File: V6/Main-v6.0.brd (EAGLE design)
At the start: 80 x 80 mm, 116 parts, among them IC1 MC34063AD, J11 AVR_SPI_PROG_3X2NS, M01 JUMPER-SMT_2_NC_PASTE_SILK, M02 JUMPER-SMT_2_NC_PASTE_SILK, M11 JUMPER-SMT_2_NC_PASTE_SILK, M12 JUMPER-SMT_2_NC_PASTE_SILK, Q1 MOSFET-NCHANNEL2N7002PW, Q2 MOSFET-NCHANNEL2N7002PW, U1 ULN2803ADWG4, U10 FSMSMTR, U2 ULN2803ADWG4, U3 UA7805CKTTR, U4 DRV8834RGERTSSOP, U5 DRV8834RGERTSSOP, U7 ATMEGA328P_TQFP, U8 SSA12, U9 FSMSMTR, X1 FH12-16S-1SH, Y1 16MHZ

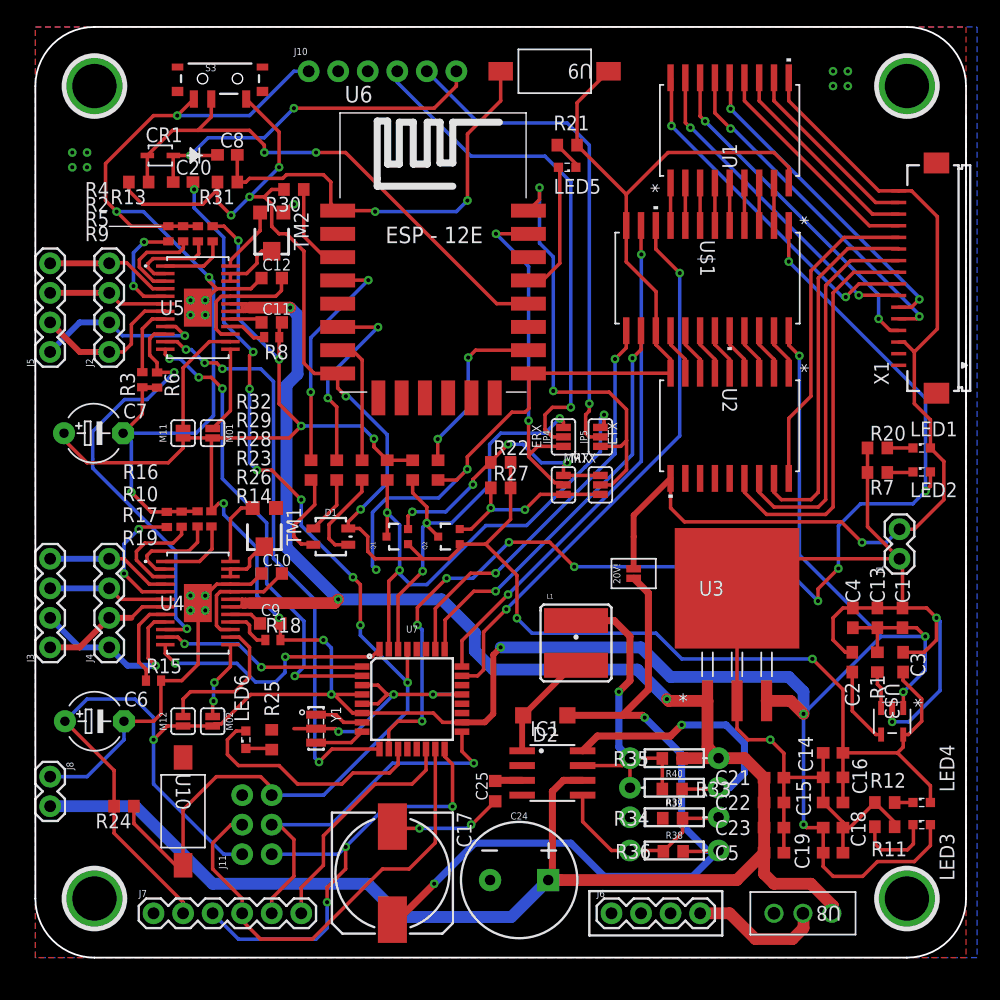
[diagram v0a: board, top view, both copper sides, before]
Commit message: Updated silkscreen in V5.1 and voltage booster is replaced in V6.0
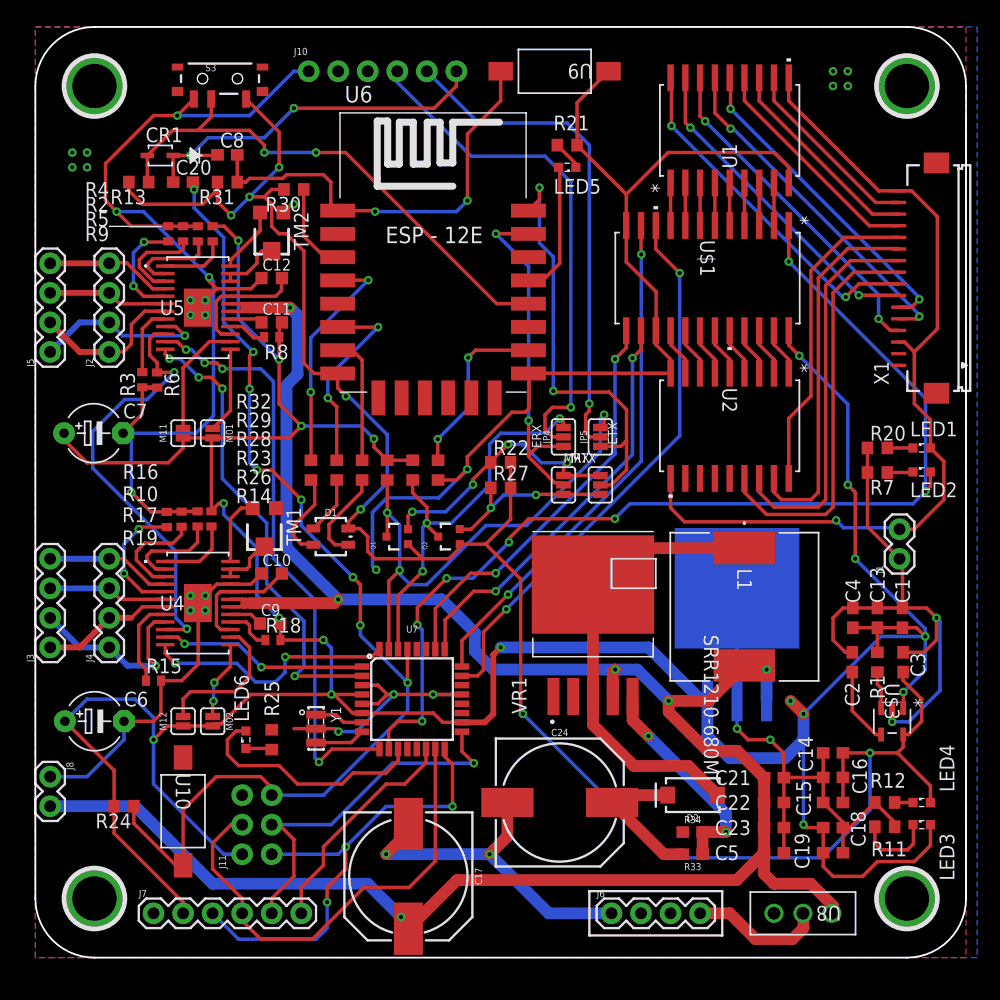
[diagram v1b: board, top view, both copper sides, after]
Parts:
- removed 20V!: JUMPER-SMT_2_NC_PASTE_NO-SILK, SparkFun-Jumpers:SMT-JUMPER_2_NC_PASTE_NO-SILK
- removed C25: 1.5nF, resistor:C0603K
- removed IC1: MC34063AD, MC34063A:SO08
- removed R35: 0.22R, resistor:R0603
- removed R36: 33k, resistor:R0603
- removed R37, R38, R39, R40: (no value), SparkFun-Resistors:AXIAL-0.3
- added VR1: XL6009, XL6009:DPAK170P1435X465-6N
- C17: value 330uF -> 220uF; device resistor:153CLV-1010 -> SparkFun-Capacitors:NIC_10X10.5_CAP
- C24: device SparkFun-Capacitors:CPOL-RADIAL-5MM-10MM -> SparkFun-Capacitors:NIC_10X10.5_CAP
- D2: value 1N5819 -> 3A/40V/500mV; device Beeclust:SOD123 -> SparkFun-DiscreteSemi:SMA-DIODE
- L1: value 180uH -> SRR1210-680M; device adjacent-reality:CR54 -> 12MM Inductor:IND_BOURNS_SRR1210
- R33: value 180R -> (none); device resistor:R0603 -> SparkFun-Resistors:0603
- R34: value 2.2k -> (none); device resistor:R0603 -> SparkFun-Resistors:0603
- moved L1 14.8 mm to (61.0, 30.2), turned to 270 degrees
- moved D2 14.4 mm to (56.5, 14.0)
- moved C24 7.53 mm to (45.1, 13.3)
- moved R33 5.87 mm to (56.5, 8.89)
- moved R34 2.09 mm to (56.5, 10.8)
- moved C17 1.40 mm to (32.1, 6.99)
- flipped U3 to the bottom
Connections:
- removed net BOOST_20: 20V!.1, C17.+, D2.C, R36.1, R38.P$2
- removed net N$37: IC1.7, L1.P$1, R33.2, R35.1, R39.P$2, R40.P$2
- removed net N$53: IC1.5, R34.2, R36.2, R37.P$2, R38.P$1
- removed net N$71: C25.2, IC1.3
- new net BOOST_FB: R33.1, R34.2, VR1.5
- net +24V: no longer 20V!.2
- net GND: now also VR1.1; no longer C25.1, IC1.2, IC1.4, R37.P$1
- net N$1: now also L1.1, VR1.3, VR1.6; no longer IC1.1, L1.P$2
- net N$2: now also C24.+, D2.C, R33.2; no longer IC1.8, R33.1, R39.P$1
- net VCC: now also C17.+, L1.2, VR1.4; no longer C24.+, IC1.6, R35.2, R40.P$1
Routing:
- net BOOST_20: track 70.5 -> 0.00 mm, vias 2 -> 0
- net N$1: track 9.41 -> 40.1 mm
- net N$37: track 28.8 -> 0.00 mm, vias 1 -> 0
- net BOOST_FB: track 0.00 -> 18.9 mm, vias 0 -> 2
- net N$53: track 16.9 -> 0.00 mm
- net +3V3: track 156.1 -> 170.1 mm
- net N$2: track 24.0 -> 13.0 mm, vias 1 -> 0
- net +24V: track 84.7 -> 74.7 mm
- net PULSE: track 99.1 -> 92.3 mm, vias 9 -> 7
- net GND: track 358.8 -> 363.8 mm, vias 31 -> 32
- net +5V: track 293.8 -> 298.5 mm, vias 15 -> 18
- net N$71: track 2.34 -> 0.00 mm
- net MOSI: track 39.7 -> 40.6 mm
- net SS_SD: track 20.4 -> 19.5 mm
- net VCC: track 191.2 -> 191.4 mm, vias 3 -> 6
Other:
- board text added: "Sprinter - Controller V6.0"
- board text removed: "Sprinter - Controller V5.1"

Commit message: Routing Cleanup V6.0
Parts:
- removed J7: (no value), SparkFun-Connectors:1X06
- removed J8: (no value), SparkFun-Connectors:1X02
- removed JP4, JP5: JUMPER-SMT_3_2-NC_PASTE_SILK, SparkFun-Jumpers:SMT-JUMPER_3_2-NC_PASTE_SILK
- C17: device SparkFun-Capacitors:NIC_10X10.5_CAP -> resistor:PANASONIC_G
- C24: device SparkFun-Capacitors:NIC_10X10.5_CAP -> resistor:PANASONIC_D
- moved C4 51.0 mm to (26.7, 2.74), turned to 0 degrees
- moved C5 37.0 mm to (26.7, 12.8), turned to 180 degrees
- moved U3 34.1 mm to (36.2, 7.62), flipped to the top, turned to 270 degrees
- moved LED3 32.8 mm to (44.5, 3.17), turned to 270 degrees
- moved LED4 32.1 mm to (45.7, 3.17), turned to 270 degrees
- moved C1 30.6 mm to (49.1, 12.1)
- moved C13 30.1 mm to (47.6, 12.1)
- moved R11 28.9 mm to (44.3, 8.26), turned to 270 degrees
- moved C17 27.9 mm to (59.4, 12.7)
- moved R12 27.1 mm to (46.4, 8.26), turned to 270 degrees
- moved C3 27.1 mm to (47.6, 23.2)
- moved U$3 26.8 mm to (47.0, 17.8)
- moved R1 26.4 mm to (46.0, 23.2)
- moved C14 26.1 mm to (43.0, 12.1), turned to 270 degrees
- moved C2 25.8 mm to (44.5, 23.2)
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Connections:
- removed net N$2: C24.+, D2.C, R33.2
- removed net N$72: J10.4, JP4.2
- removed net N$81: J10.5, JP5.2
- net +24V: now also C24.+, D2.C, R33.2
- net +5V: no longer J7.2
- net ESPRX: now also J10.4; no longer JP4.1
- net ESPTX: now also J10.5; no longer JP5.1
- net GND: no longer J7.1, J8.1
- net MEGARX: no longer JP4.3
- net MEGATX: no longer JP5.3
- net MISO: no longer J7.3
- net MOSI: no longer J7.4
- net SCK: no longer J7.5
- net SS_SD: no longer J7.6
- net VCC: no longer J8.2
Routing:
- net GND: track 363.8 -> 21.7 mm, vias 32 -> 14
- net N$72: track 44.4 -> 0.00 mm, vias 1 -> 0
- net N$81: track 42.9 -> 0.00 mm, vias 1 -> 0
- net MEGATX: track 44.7 -> 13.2 mm, vias 3 -> 0
- net VCC: track 191.4 -> 160.0 mm, vias 6 -> 7
- net +3V3: track 170.1 -> 139.5 mm, vias 7 -> 8
- net +24V: track 74.7 -> 103.2 mm, vias 1 -> 2
- net +5V: track 298.5 -> 274.2 mm, vias 18 -> 11
- net MEGARX: track 35.8 -> 13.5 mm
- net ESPRX: track 30.4 -> 52.0 mm, vias 2 -> 3
- net SS_SD: track 19.5 -> 0.00 mm
- net MISO: track 41.3 -> 24.2 mm, vias 3 -> 1
- net RST: track 93.5 -> 110.5 mm, vias 8 -> 2
- net N$1: track 40.1 -> 24.7 mm
- net MOSI: track 40.6 -> 26.9 mm, vias 0 -> 1
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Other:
- board text added: "BOOT"
- board text added: "GND"
- board text added: "PGM"
- board text added: "RX"
- board text added: "TX"

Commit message: V6.0 Updated
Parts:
- J2, J3, J4, J5: device SparkFun-Connectors:1X04 -> SparkFun-Connectors:1X05
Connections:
- removed net GND: C1.2, C10.1, C12.1, C13.2, C14.2, C15.2, C16.2, C17.-, C18.2, C19.2, C2.2, C21.2, C22.2, C23.2, C24.-, C3.2, C4.2, C5.2, C6.-, C7.-, J1.1, J10.1, J11.6, J6.1, R10.2, R11.1, R12.1, R14.1, R15.2, R16.2, R17.2, R2.2, R20.1, R21.1, R25.1, R3.2, R34.1, R4.2, R5.2, R6.2, R7.1, S3.1, TM1.1, TM2.1, U$1.12, U$1.15, U$3.2, U1.9, U10.1, U2.9, U3.2, U3.4, U4.21, U4.EPAD, U5.21, U5.EPAD, U6.GND, U7.21, U7.3, U7.5, U9.1, VR1.1, Y1.2
- new net GND_ABC: C1.2, C10.1, C12.1, C13.2, C14.2, C15.2, C16.2, C17.-, C18.2, C19.2, C2.2, C21.2, C22.2, C23.2, C24.-, C3.2, C4.2, C5.2, C6.-, C7.-, J1.1, J10.1, J11.6, J2.5, J3.5, J4.5, J5.5, J6.1, R10.2, R11.1, R12.1, R14.1, R15.2, R16.2, R17.2, R2.2, R20.1, R21.1, R25.1, R3.2, R34.1, R4.2, R5.2, R6.2, R7.1, S3.1, TM1.1, TM2.1, U$1.12, U$1.15, U$3.2, U1.9, U10.1, U2.9, U3.2, U3.4, U4.21, U4.EPAD, U5.21, U5.EPAD, U6.GND, U7.21, U7.3, U7.5, U9.1, VR1.1, Y1.2
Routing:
- net GND_ABC: track 0.00 -> 41.7 mm, vias 0 -> 17
- net GND: track 21.7 -> 0.00 mm, vias 14 -> 0
- net VCC: track 160.0 -> 160.8 mm
- added copper zone on layer 1, net GND_ABC
- added copper zone on layer 16, net GND_ABC
- removed copper zone on layer 1, net GND
- removed copper zone on layer 16, net GND

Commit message: V6.0 Updated
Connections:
- net GND_ABC renamed GND
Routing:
- net N$1: vias 0 -> 41
- net GND: vias 17 -> 62
- added copper zone on layer 16, net N$1
